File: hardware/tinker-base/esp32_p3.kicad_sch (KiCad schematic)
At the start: 34 parts, among them J8 CON-SMA-EDGE-S, U1 GD25Q128ESIG, U15 479480001, U16 E220-900MM22S, U3 ESP32-S3RH2, Y1 ABS07-32.768KHZ-T, Y2 ECS-400-10-37B2-CKY-TR

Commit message: hardware(Tinker-Base): the Beetle/Mantis chip antenna and WLCSP boot flash, with C24 and the GPIO0/RXEN pulls, placed and routed; J2/R13/R16 relinked (#1545)
The ESP32-S3 sheet takes on the newer parts the Beetle and Mantis carry,
plus the decoupling Espressif's hardware checklist asks for:
- U15 becomes the AANI-CH-0070 edge-mounted chip antenna, with the flight
  computers' pi match: C7 5.1 pF in series, L4 2.2 nH to ground (it was
  the old antenna's 4.3 nH shunt), and C5, an unfitted shunt kept for
  tuning. The RF netclass pattern follows the feed net, Net-(C5-Pad1).
- U1 becomes the W25Q128JVYIQ 24-ball WLCSP NOR on +3V3, replacing the
  GD25Q128ESIG SOIC-8 on VDD_SPI, with C1 beside it. VDD_SPI keeps C9, and
  C10 stays at 10 µF: the LoRa review's finding 4a applies here too.
- C24 adds 10 µF on VDD3P3. R5 is a 10 k GPIO0 pull-up. R6 is a 100 k
  L_RXEN pull-down, because GPIO35 has no reset pull.
U1 and U15 keep their symbol uuids, so Update PCB swapped their
footprints in place.

Layout:
- The antenna sits at the left edge, inside a keep-out on all four copper
  layers.
- The flash escapes at 0.1 mm in its ball channels. CLK and WP cross the
  other flash lines on B.Cu.
- C24 sits above C16, and R1 moved beside C8 to make room. R5 and R6 sit
  beside their pins.
- J2, R13 and R16 are linked to their symbols again. The committed board
  had J2 with no path, and R13/R16 with the root sheet's uuid in front,
  so Update PCB had parked fresh copies off the board. The linked copies
  now sit at the committed positions, and the old tracks reconnect.
- The owner's later touches are kept: the logo, and two B.Cu tracks
  (Net-(U22-ON) and L_RXEN) nudged 0.18 mm.

Zones are refilled with the project's rules, at the owner's request,
using kicad-cli in a project mirror. The saved file's fills predated the
two nudged tracks, so the B.Cu GND pour overlapped Net-(U22-ON). The
refill differs from the saved board in its 30 filled_polygon blocks
alone, and a second refill rep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
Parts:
- added C24: 10 uF, Capacitor_SMD:C_0402_1005Metric, symbol Device:C
- added C5: DNP, Capacitor_SMD:C_0402_1005Metric, symbol Device:C
- added C7: 5.1 pF, Capacitor_SMD:C_0402_1005Metric, symbol Device:C
- added R5: 10 k, Resistor_SMD:R_0402_1005Metric, symbol Device:R_US
- added R6: 100 k, Resistor_SMD:R_0402_1005Metric, symbol Device:R_US
- L4: value 4.3 nH -> 2.2 nH; MPN LQW15AN4N3C00D -> LQW15AN2N2C10
- U1: value GD25Q128ESIG -> W25Q128JVYIQ; footprint Footprints:SOIC127P790X216-8N -> Footprints:24-WLCSP_Y_WIN; symbol Custom:W25Q128JVSIQ -> Custom:W25Q128JVYIQ; MPN GD25Q128ESIG -> W25Q128JVYIQ; Mfr GigaDevice -> Winbond
- U15: value 479480001 -> AANI-CH-0070; footprint Footprints:ANT_47948-0001_MOL -> Footprints:ANT_AANI-CH-0070_ABR; symbol Custom:479480001 -> Custom:AANI-CH-0070; MPN 479480001 -> AANI-CH-0070; Mfr Molex -> Abracon
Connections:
- net +3V3: now also C1.1, U1.B2 (VCC), R5.2
- net GND: now also U1.E3 (GND), U15.2 (GND), U15.3 (GND), C24.2, C5.2, R6.2; no longer U1.4 (GND)
- net L_RXEN: now also R6.1
- net SPI_CLK: now also U1.D2 (CLK); no longer U1.6 (CLK)
- net SPI_CS0: now also U1.B3 (/CS); no longer U1.1 (/CS)
- net SPI_D: now also U1.E2 (DI(IO0)); no longer U1.5 (DI_(IO0))
- net SPI_HD: now also U1.C2 (/HOLD(IO3)); no longer U1.7 (/HOLD_or_/RESET_(IO3))
- net SPI_Q: now also U1.C3 (DO(IO1)); no longer U1.2 (DO_(IO1))
- net SPI_WP: now also U1.D3 (/WP(IO2)); no longer U1.3 (IO2)
- net VDD_SPI: no longer C1.1, U1.8 (VCC)
- net at C16.1, L3.1, U3.2 (VDD3P3)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: now also C24.1
- net at U15.1 (FEED): now also U15.4 (FEED), C5.1, C7.1
- net at L4.2, U3.1 (LNA_IN): now also C7.2; no longer U15.4 (Feed)
- net at S3.1, U3.5 (GPIO0): now also R5.1
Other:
- moved on the sheet: C1, C17, C18, C19, L3

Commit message: hardware(Tinker-Base): V1 design review and fixes -- the antenna window clear on every layer, 21 ground vias, L5/C25/fiducials, R52 1.2 k, and fab notes for the order
Stacked on #1545 (the Beetle/Mantis parts). The V1 JLC package was plotted from
exactly this board (md5 1fe1e414).

The review is new: hardware/tinker-base/design-review-2026-09-28.md. It has a
table of the fixes applied, and of the items left undone with the reason for each.

Layout (tinker-base.kicad_pcb):
- U15 antenna. F.Cu keeps the feed notch. A second rule area clears In1, In2 and
  B.Cu under the whole 4.6 x 3.0 mm window. Before this, In1 GND, In2 +3V3 and
  B.Cu GND filled under the feed pads. Nine GND fence vias.
- 21 GND vias: nine beside signal vias (signal vias more than 1 mm from a
  ground via: 14 -> 5), nine in U3's exposed pad between its paste windows, one
  for C16/C24 and two for U16's ground pads. Five old vias removed.
- J8 moved so its pads start 0.30 mm inside the edge. L5 (330 nH) runs from the
  SMA line to GND beside it.
- C25 (100 nF) on V_SWITCH at U9.
- J2's signal pads trimmed to HRO's land, in the library too. BT2.P to J2 goes
  from 0.40 to 0.84 mm.
- S3 gets an F.Cu keep-out over its body, and its GPIO0 via moves out from
  under it.
- Thermal reliefs on J2's shell legs and D6's cathode. Pin-1 dots on U3, U5, U22,
  CR1 and U16. FID1-FID3 added, R13/R16 refs hidden, and a B.Silk "-" at BT2's
  N end.
- Zones refilled. A second kicad-cli refill reproduces them byte for byte.

Schematic:
- L5, C25 and FID1-FID3 added.
- R52 680 -> 1.2 k. The charge current drops from 0.79 A to about 0.45 A, so the
  charger's heat no longer trips the board-mounted NTC from room temperature.
- Title blocks, rev V1, on all four sheets.
- bom.csv regenerated.

Library:
- IC_ESP32-S3 and 8L_WSON_8x6x3p4x4p3_MAC go back to their window polygons.
  4078070b had added paste pads on top of those polygons.
- USB_C_HRO_TYPE-C-31-M-12 pads trimmed.
- ANT_AANI-CH-0070_ABR's description states the r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
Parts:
- added L5: 330 nH, Inductor_SMD:L_0603_1608Metric, symbol Device:L_Small
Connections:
- net GND: now also L5.1
- net at J8.1, U16.6 (ANT): now also L5.2
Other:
- company: (none) -> TinkerRocket
- title: (none) -> tinker-base: ESP32-S3
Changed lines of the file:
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@@
 	(generator_version "10.0")
 	(paper "A4")
+	(title_block
+		(title "tinker-base: ESP32-S3")
+		(date "2026-09-28")
+		(rev "V1")
+		(company "TinkerRocket")
+	)
 	(text "Strapping Pins:\nGPIO 0  (internal pull up)\nGPIO 3  (JTAG selection)\nGPIO 45 (internal pull down)\nGPIO 46 (pull down at boot)\n"
 		(exclude_from_sim no)
@@
 	(wire
 		(pts
-			(xy 45.72 173.99) (xy 67.31 173.99)
+			(xy 45.72 173.99) (xy 50.8 173.99)
 		)
 		(stroke
@@
 	(wire
 		(pts
+			(xy 50.8 173.99) (xy 67.31 173.99)
+		)
+		(stroke
+			(width 0)
+			(type default)
+		)
+	)
+	(junction
+		(at 50.8 173.99)
+		(diameter 0)
+		(color 0 0 0 0)
+	)
+	(wire
+		(pts
 			(xy 172.72 41.275) (xy 171.45 41.275)
 		)
@@
 					(unit 1)
 				)
+			)
+		)
+	)
+	(symbol
+		(lib_id "Device:L_Small")
+		(at 50.8 171.45 0)
+		(unit 1)
+		(body_style 1)
+		(exclude_from_sim no)
+		(in_bom yes)
+		(on_board yes)
+		(in_pos_files yes)
+		(dnp no)
+		(property "Reference" "L5"
+			(at 52.705 170.815 0)
+			(show_name no)
+			(do_not_autoplace no)
+			(effects
+				(font
+					(size 1.27 1.27)
+				)
+			)
+		)
+		(property "Value" "330 nH"
+			(at 52.705 172.72 0)
+			(show_name no)
+			(do_not_autoplace no)
+			(effects
+				(font
+					(size 1.27 1.27)
+				)
+			)
+		)
+		(property "Footprint" "Inductor_SMD:L_0603_1608Metric"
+			(at 50.8 171.45 0)
+			(hide yes)
+			(show_name no)
+			(do_not_autoplace no)
+			(effects
+				(font
+					(size 1.27 1.27)
+				)
+			)
+		)
+		(property "Datasheet" ""
+			(at 50.8 171.45 0)
+			(hide yes)
+			(show_name no)
+			(do_not_autoplace no)
+			(effects
+				(font
+					(size 1.27 1.27)
+				)
+			)
+		)
+		(property "Description" "Inductor, small symbol"
+			(at 50.8 171.45 0)
+			(hide yes)
+			(show_name no)
+			(do_not_autoplace no)
+			(effects
+				(font
+					(size 1.27 1.27)
+				)
+			)
+		)
+		(property "MPN" "LQW18ANR33G00D"
+			(at 50.8 171.45 0)
+			(hide yes)
+			(show_name no)
+			(do_not_autoplace no)
+			(effects
+				(font
+					(size 1.27 1.27)
+				)
+			)
+		)
+		(property "Mfr" "Murata"
+			(at 50.8 171.45 0)
+			(hide yes)
+			(show_name no)
+			(do_not_autoplace no)
+			(effects
+				(font
+					(size 1.27 1.27)
+				)
+			)
+		)
+		(pin "1"
+		)
+		(pin "2"
+		)
+		(instances
+			(project "tinker-base"
+				(path "/d2421514-d142-4c71-ac69-48d30c1a771f/6cfb856e-ef45-4f36-bd7e-e27b13a29501"
+					(reference "L5")
+					(unit 1)
+				)
+			)
+		)
+	)
+	(symbol
+		(lib_id "power:GND")
+		(at 50.8 168.91 180)
+		(unit 1)
+		(body_style 1)
+		(exclude_from_sim no)
+		(in_bom yes)
+		(on_board yes)
+		(in_pos_files yes)
+		(dnp no)
+		(fields_autoplaced yes)
+		(property "Reference" "#PWR0237"
+			(at 50.8 162.56 0)
+			(hide yes)
+			(show_name no)
+			(do_not_autoplace no)
+			(effects
+				(font
+					(size 1.27 1.27)
+				)
+			)
+		)
+		(property "Value" "GND"
+			(at 50.8 164.465 0)
+			(show_name no)
+			(do_not_autoplace no)
+			(effects
+				(font
+					(size 1.27 1.27)
+				)
+			)
+		)
+		(property "Footprint" ""
+			(at 50.8 168.91 0)
+			(hide yes)
+			(show_name no)
+			(do_not_autoplace no)
+			(effects
+				(font
+					(size 1.27 1.27)
+				)
+			)
+		)
+		(property "Datasheet" ""
+			(at 50.8 168.91 0)
+			(hide yes)
+			(show_name no)
+			(do_not_autoplace no)
+			(effects
+				(font
+					(size 1.27 1.27)
+				)
+			)
+		)
+		(property "Description" ""
+			(at 50.8 168.91 0)
+			(hide yes)
+			(show_name no)
+			(do_not_autoplace no)
+			(effects
+				(font
+					(size 1.27 1.27)
+				)
+			)
+		)
+		(pin "1"
+		)
+		(instances
+			(project "tinker-base"
+				(path "/d2421514-d142-4c71-ac69-48d30c1a771f/6cfb856e-ef45-4f36-bd7e-e27b13a29501"
+					(reference "#PWR0237")
+					(unit 1)
+				)

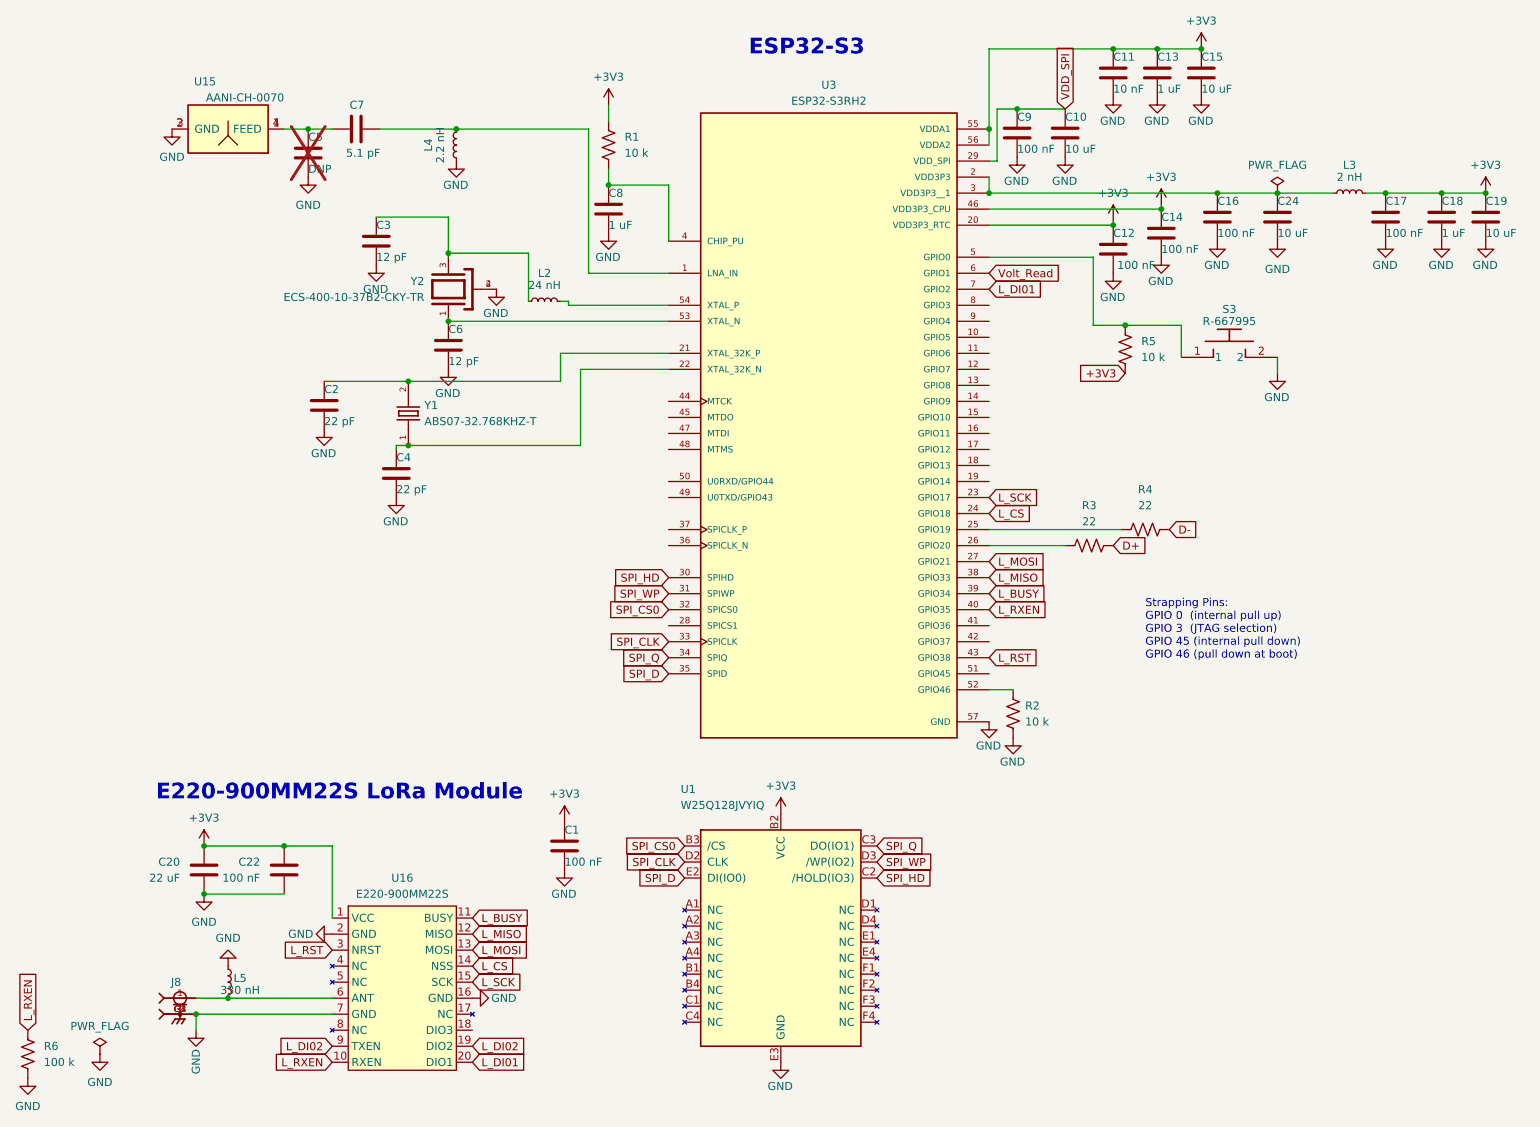
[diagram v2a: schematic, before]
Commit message: hardware(Tinker-Base V2): in-package flash, a log flash, the GCT USB-C, 330 R LED resistors and a fixed 3.3 V buck, schematic and layout (#1685)
V2 of the base station, in work (title blocks V2; V1 is tag tinker-base-v1.0.0).

- U3 is an ESP32-S3FH4R2 (4 MB flash + 2 MB PSRAM in the package); the WLCSP
  boot NOR U1 and its C1 are gone.
- U23, a GD25Q128ESIGR log flash, on GPIO4-7 (SPI3, the V2 base station's NAND
  pins), with R58-R60 pull-ups and C89.
- J2 is the GCT USB4110-GF-A, placed so its front face sits where HRO's did.
- R41/R54 LED resistors 330 R.
- U9 is the TPS62152RGTR fixed 3.3 V buck (as the Beetle/Mantis), replacing the
  TPS63020 and its R13/R16 divider. The first V1 board ran +3V3 at 6.4 V; its
  U9 symbol carried a stale MP = TPS63021DSJR. DEF to GND for 3.3 V; C90 soft
  start. The fab notes ask for LCSC C2070611 by code.
- PCB brought up to the schematic: buck re-laid, U23 placed and routed (SCK
  hops to B.Cu), U1's escapes removed, Volt_Read re-routed on B.Cu, J2 on the
  GCT land. DRC with schematic parity: 0 errors, 0 unconnected, 0 parity
  issues; 26 warnings as at V1's sign-off. check_board_parity passes.

Not done: gerbers/position file, bom.csv and the fab-notes order block (for a
V2 order), and the base-station firmware for the 4 MB table and the external
log flash. README *Status* has the details.

Co-authored-by: Claude Opus 5.5 <noreply@anthropic.com>
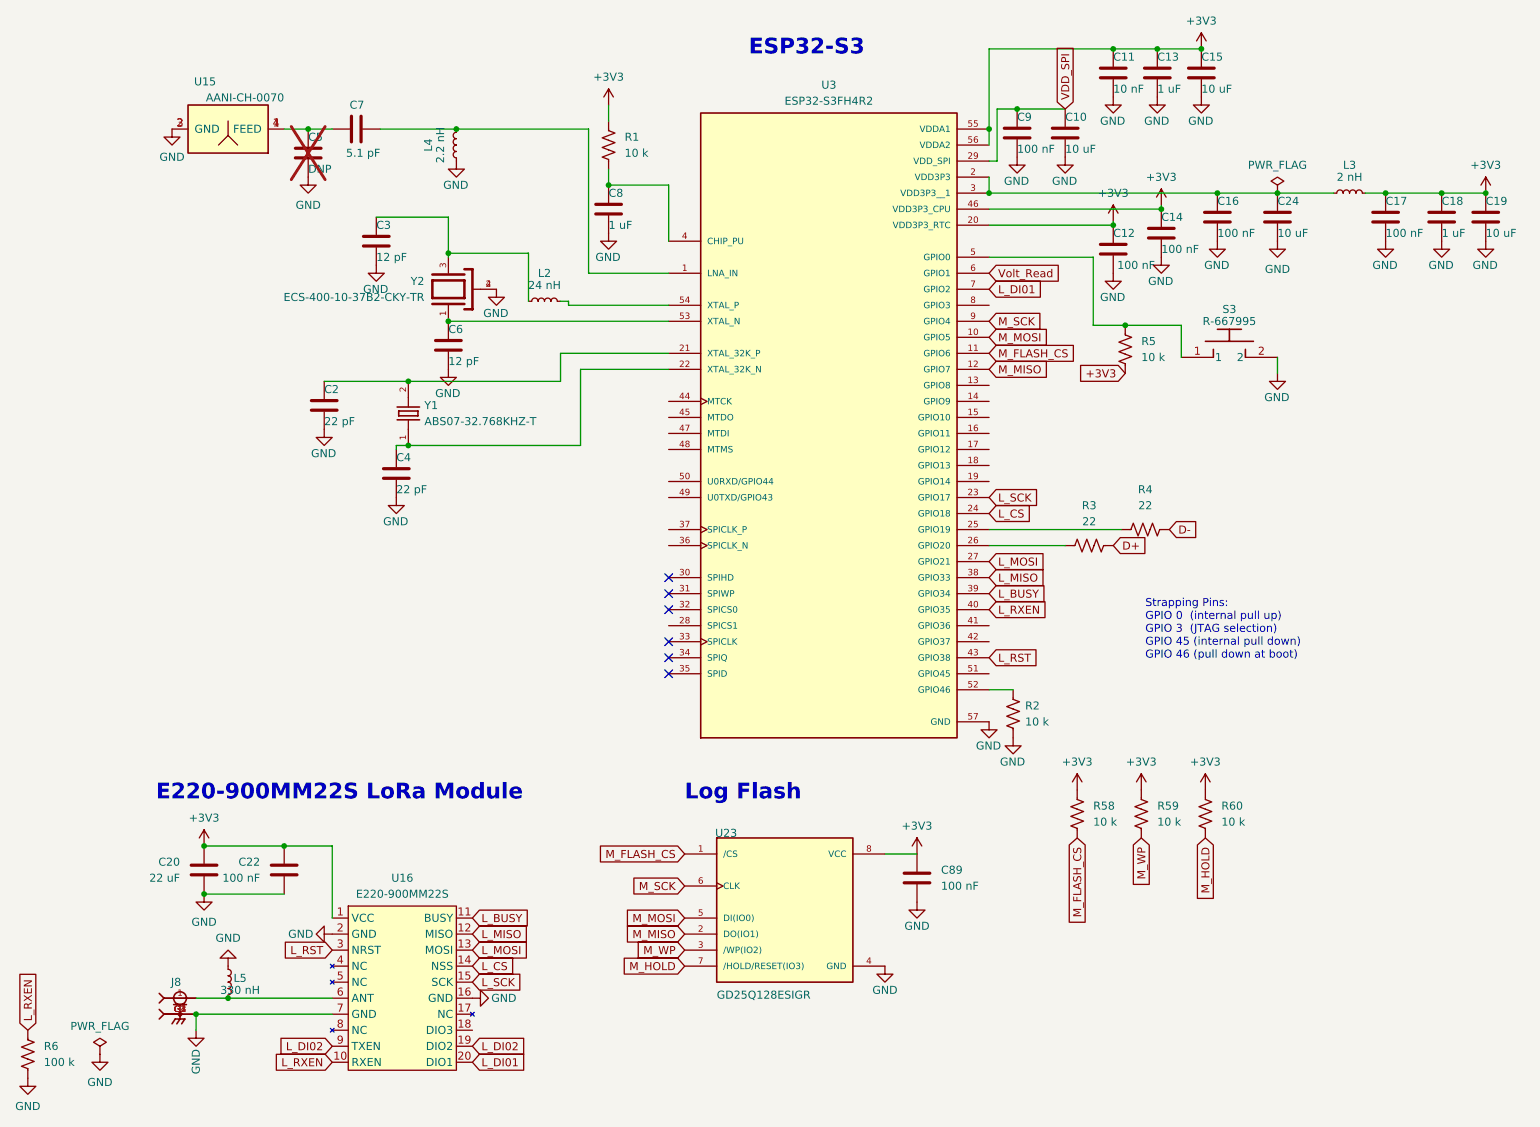
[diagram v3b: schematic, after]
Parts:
- removed C1: 100 nF, Capacitor_SMD:C_0402_1005Metric, symbol Device:C
- removed U1: W25Q128JVYIQ, Footprints:24-WLCSP_Y_WIN, symbol Custom:W25Q128JVYIQ
- added C89: 100 nF, Capacitor_SMD:C_0402_1005Metric, symbol Device:C
- added R58, R59, R60: 10 k, Resistor_SMD:R_0402_1005Metric, symbol Device:R_US
- added U23: GD25Q128ESIGR, Footprints:SOIC127P790X216-8N, symbol Custom:W25Q128JVSIQ
- U3: value ESP32-S3RH2 -> ESP32-S3FH4R2; MPN ESP32-S3RH2 -> ESP32-S3FH4R2
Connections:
- net +3V3: now also C89.1, R58.1, R59.1, R60.1, U23.8 (VCC)
- net GND: now also C89.2, U23.4 (GND)
- net M_MOSI: now reaches U3.10 (GPIO5)
- net M_MOSI: now also U23.5 (DI(IO0))
- net M_FLASH_CS: now reaches U3.11 (GPIO6)
- net M_FLASH_CS: now also R58.2, U23.1 (/CS)
- net M_MISO: now reaches U3.12 (GPIO7)
- net M_MISO: now also U23.2 (DO(IO1))
- net M_SCK: now reaches U3.9 (GPIO4)
- net M_SCK: now also U23.6 (CLK)
- net SPI_CLK: no longer names the net of U3.33 (SPICLK)
- net SPI_CS0: no longer names the net of U3.32 (SPICS0)
- net SPI_D: no longer names the net of U3.35 (SPID)
- net SPI_HD: no longer names the net of U3.30 (SPIHD)
- net SPI_Q: no longer names the net of U3.34 (SPIQ)
- net SPI_WP: no longer names the net of U3.31 (SPIWP)
- new net M_HOLD: R60.2, U23.7 (/HOLD/RESET(IO3))
- new net M_WP: R59.2, U23.3 (/WP(IO2))
- no-connect marks 0 -> 6
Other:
- note added: "Log Flash"
